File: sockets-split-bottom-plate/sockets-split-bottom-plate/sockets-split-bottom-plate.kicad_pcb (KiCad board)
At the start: 2 copper layers, 138.1 x 85.4 mm, 0 parts

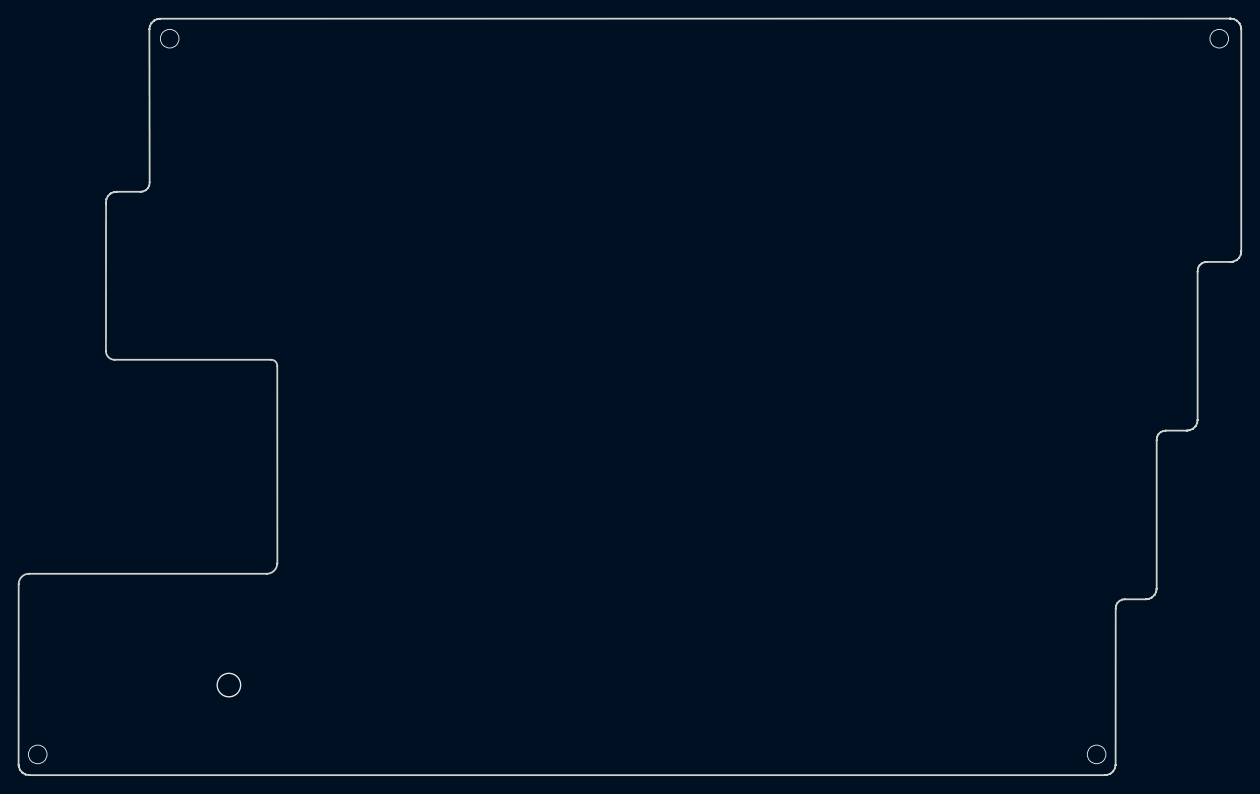
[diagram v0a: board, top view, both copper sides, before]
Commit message: Add solder layer & Fix document
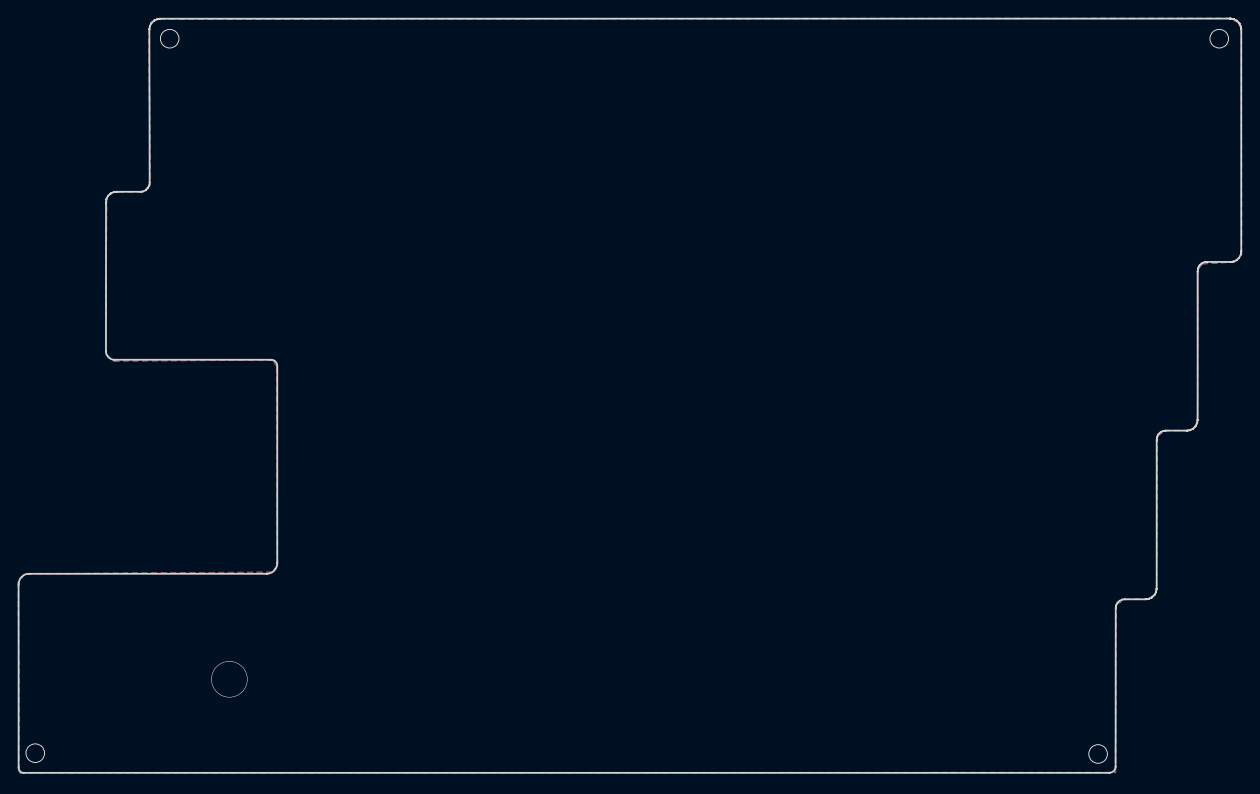
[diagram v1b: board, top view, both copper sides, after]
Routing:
- added copper zone on B.Cu, net (none)
- added copper zone on F.Cu, net (none)
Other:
- board size 138.1 x 85.4 mm -> 138.1 x 85.2 mm

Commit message: Update docs
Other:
- board size 138.1 x 85.2 mm -> 138.1 x 84.6 mm
